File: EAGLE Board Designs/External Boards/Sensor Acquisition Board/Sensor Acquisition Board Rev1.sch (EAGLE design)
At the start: 15 parts, among them U1 ATMEGA328P-AU, X1 CONNECTOR-4NANO-FIT_RIGHT_ANG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

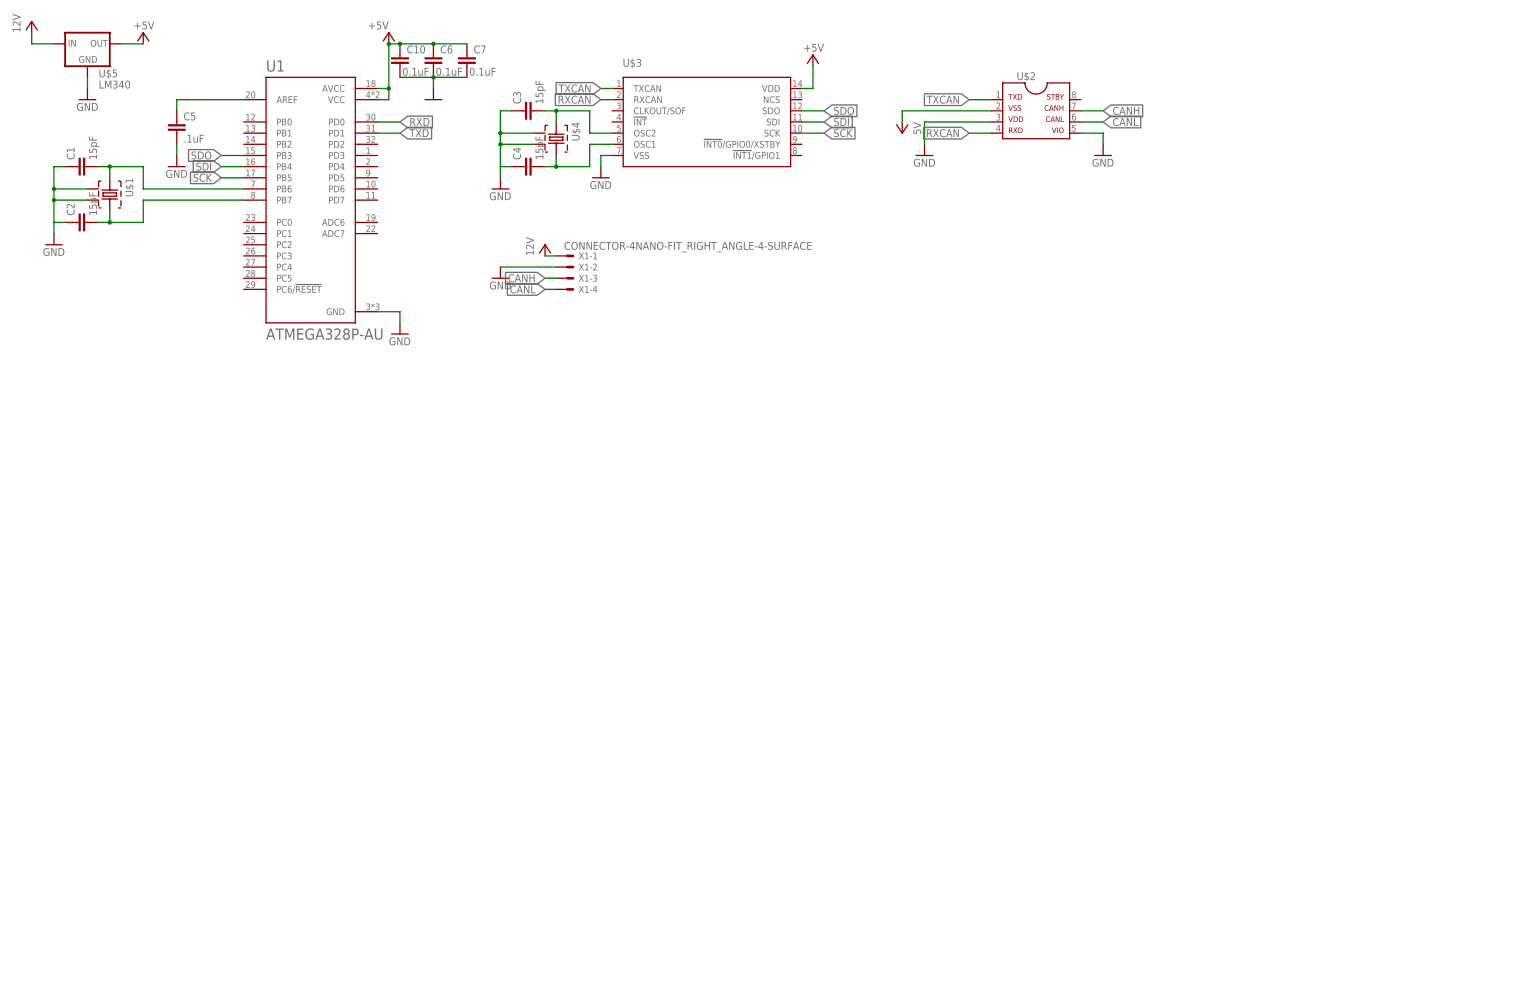
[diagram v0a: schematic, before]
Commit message: Fnished schematic (completed the signal processing portion) and made board
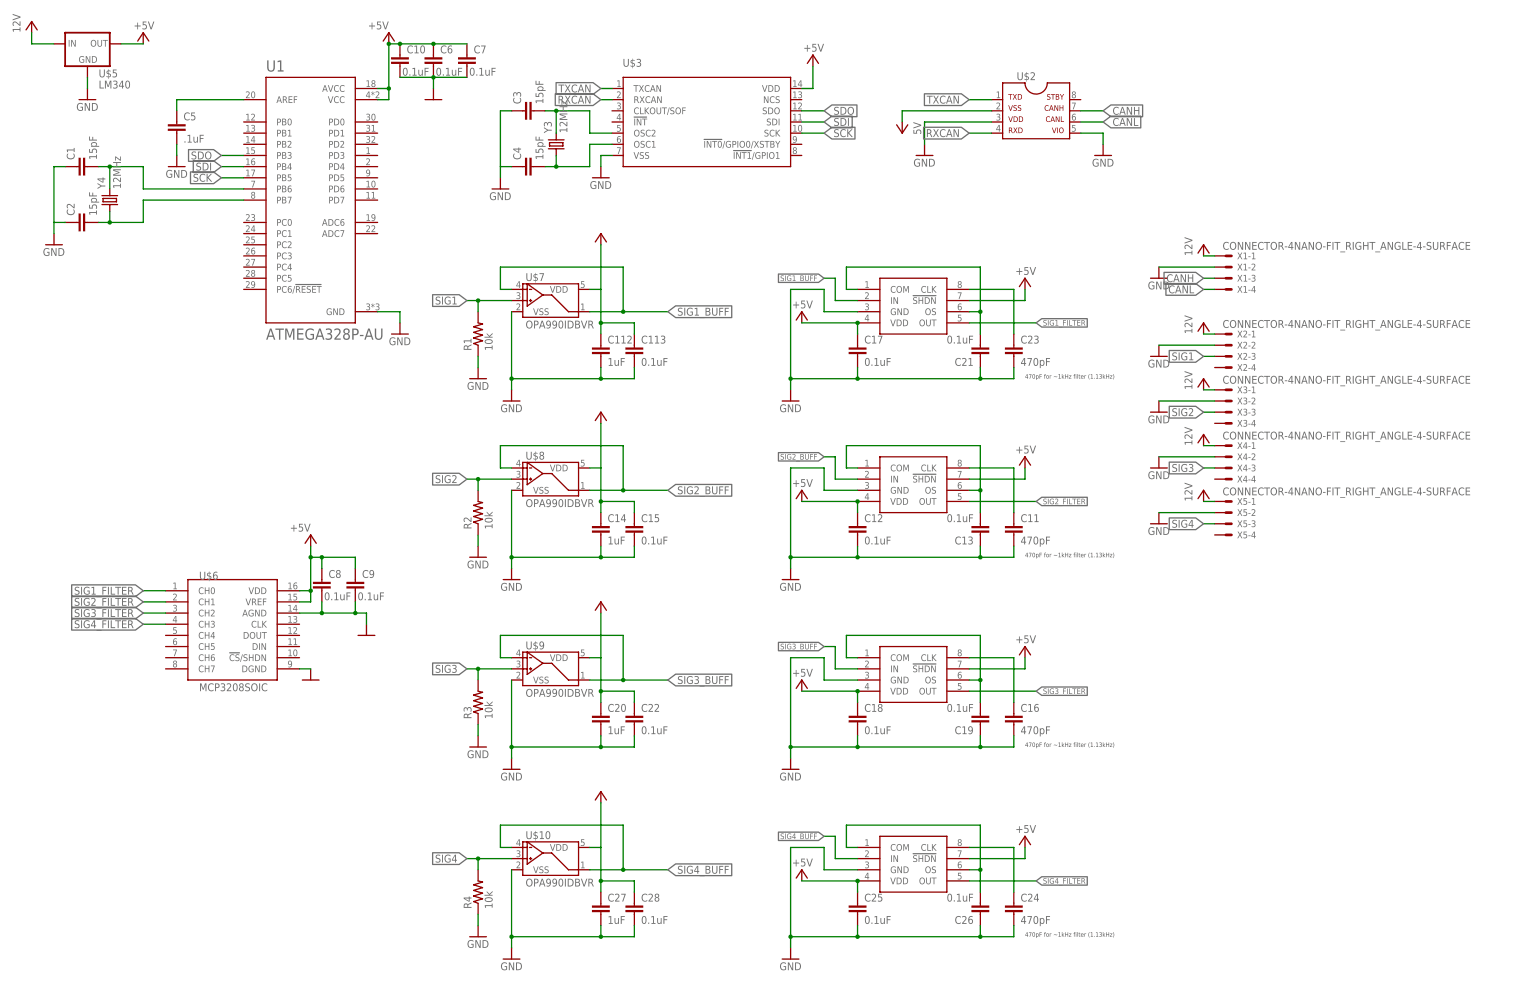
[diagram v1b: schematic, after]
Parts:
- removed U$1, U$4: (no value), HyTechDevices:ABM3B
- added C11, C16, C23, C24: 470pF, HyTechDevices:CAP0603-CAP
- added C112, C14, C20, C27: 1uF, HyTechDevices:CAP0603-CAP
- added C113, C12, C13, C15, C17, C18, C19, C21, C22, C25, C26, C28, C8, C9: 0.1uF, HyTechDevices:CAP0603-CAP
- added R1, R2, R3, R4: 10k, HyTechDevices:RESISTOR1206
- added U$10, U$7, U$8, U$9: OPA990IDBVR, HyTechDevices:OPA990IDBVR
- added U$6: MCP3208SOIC, HyTechDevices:MCP3208SOIC
- added U2, U24, U3, U4: MAX7480, HyTechDevices:MAX7480
- added X2, X3, X4, X5: CONNECTOR-4NANO-FIT_RIGHT_ANGLE-4-SURFACE, HyTechDevices:CONNECTOR-4NANO-FIT_RIGHT_ANGLE-4-SURFACE
- added Y3, Y4: 12MHz, HyTechDevices:CRYSTALCRYSTAL-SMD-5X3-12MHZ
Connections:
- removed net RXD: U1.PD0
- removed net TXD: U1.PD1
- new net N$10: C19.2, U3.COM, U3.OS
- new net N$11: C24.1, U4.CLK
- new net N$12: C26.2, U4.COM, U4.OS
- new net N$136: C23.1, U24.CLK
- new net N$142: C21.2, U24.COM, U24.OS
- new net N$6: C11.1, U2.CLK
- new net N$7: C13.2, U2.COM, U2.OS
- new net N$9: C16.1, U3.CLK
- new net SIG1: R1.2, U$7.VIN+, X2-3.S
- new net SIG1_BUFF: U$7.VIN-, U$7.VOUT, U24.IN
- new net SIG1_FILTER: U$6.CH0, U24.OUT
- new net SIG2: R2.2, U$8.VIN+, X3-3.S
- new net SIG2_BUFF: U$8.VIN-, U$8.VOUT, U2.IN
- new net SIG2_FILTER: U$6.CH1, U2.OUT
- new net SIG3: R3.2, U$9.VIN+, X4-3.S
- new net SIG3_BUFF: U$9.VIN-, U$9.VOUT, U3.IN
- new net SIG3_FILTER: U$6.CH2, U3.OUT
- new net SIG4: R4.2, U$10.VIN+, X5-3.S
- new net SIG4_BUFF: U$10.VIN-, U$10.VOUT, U4.IN
- new net SIG4_FILTER: U$6.CH3, U4.OUT
- net +5V: now also C112.1, C113.1, C12.1, C14.1, C15.1, C17.1, C18.1, C20.1, C22.1, C25.1, C27.1, C28.1, C8.1, C9.1, U$10.VDD, U$6.VDD, U$6.VREF, U$7.VDD, U$8.VDD, U$9.VDD, U2.!SHDN, U2.VDD, U24.!SHDN, U24.VDD, U3.!SHDN, U3.VDD, U4.!SHDN, U4.VDD
- net GND: now also C11.2, C112.2, C113.2, C12.2, C13.1, C14.2, C15.2, C16.2, C17.2, C18.2, C19.1, C20.2, C21.1, C22.2, C23.2, C24.2, C25.2, C26.1, C27.2, C28.2, C8.2, C9.2, R1.1, R2.1, R3.1, R4.1, U$10.VSS, U$6.AGND, U$6.DGND, U$7.VSS, U$8.VSS, U$9.VSS, U2.GND, U24.GND, U3.GND, U4.GND, X2-2.S, X3-2.S, X4-2.S, X5-2.S
- net N$1: no longer U$1.2, U$1.4, U$4.2, U$4.4
- net N$2: now also Y4.2; no longer U$1.1
- net N$3: now also Y4.1; no longer U$1.3
- net N$4: now also Y3.2; no longer U$4.1
- net N$5: now also Y3.1; no longer U$4.3
- net VCC: now also X2-1.S, X3-1.S, X4-1.S, X5-1.S
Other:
- note added: "470pF for ~1kHz filter (1.13kHz)"
- moved on the sheet: X1-1, X1-2, X1-3, X1-4

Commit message: Added controls and connectors
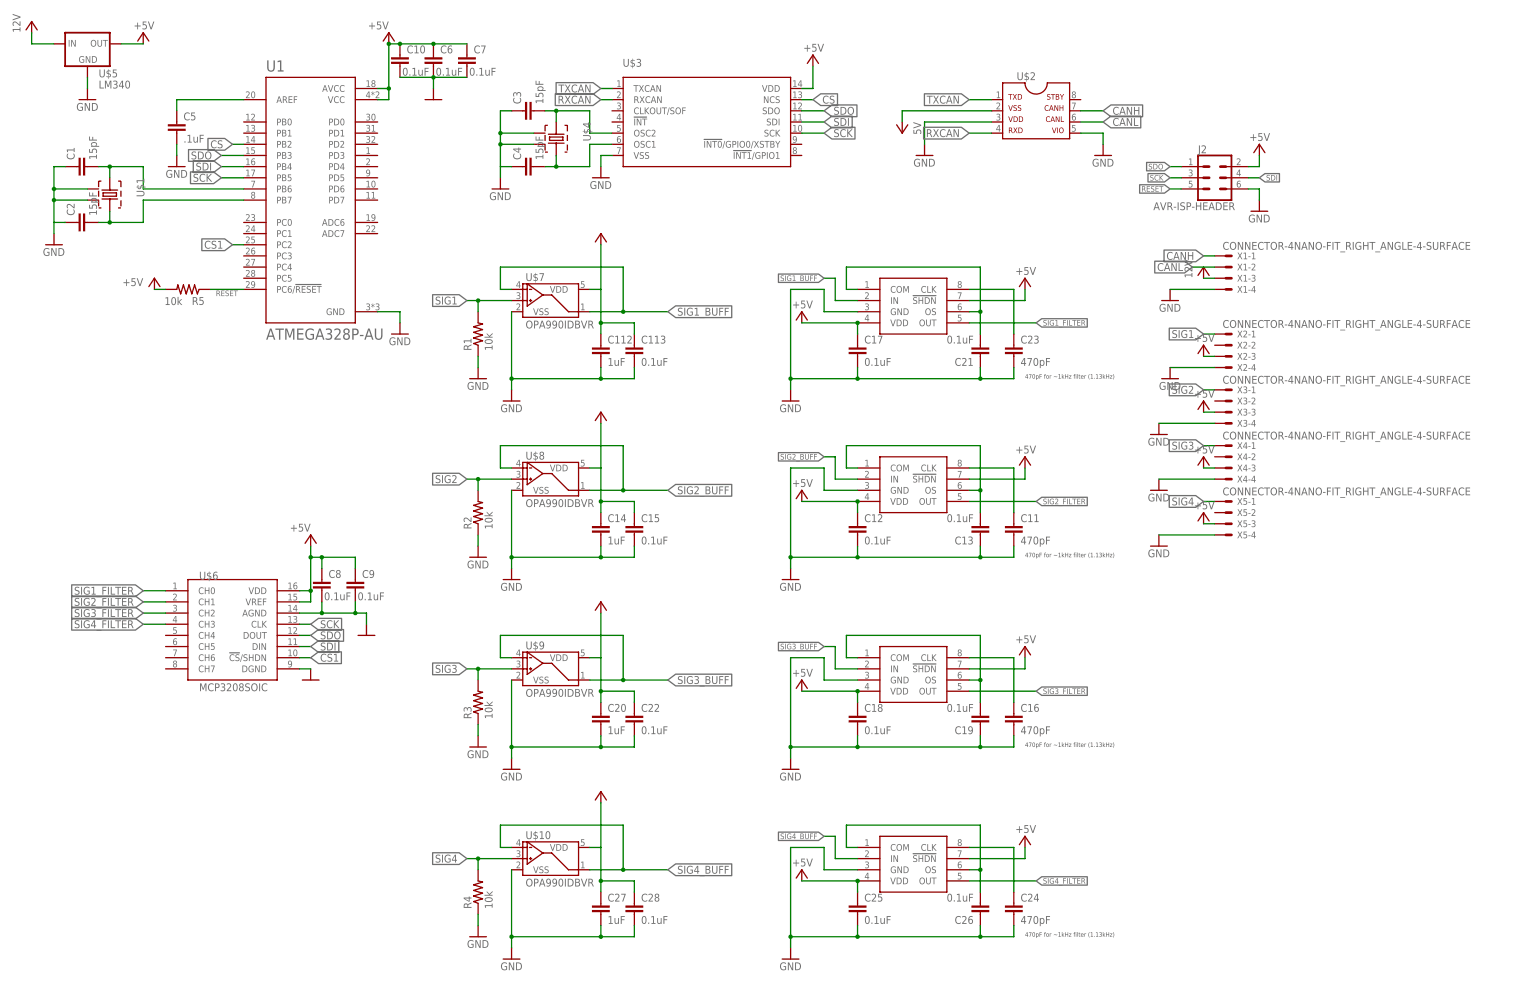
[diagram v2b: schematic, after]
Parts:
- removed Y3, Y4: 12MHz, HyTechDevices:CRYSTALCRYSTAL-SMD-5X3-12MHZ
- added J2: AVR-ISP-HEADER, HyTechDevices:AVR-ISP-HEADER
- added R5: 10k, HyTechDevices:RESISTOR0603
- added U$1, U$4: (no value), HyTechDevices:ABM3B
- C1, C2, C3, C4: device HyTechDevices:CAP1210 -> HyTechDevices:CAP0603-CAP
- R1, R2, R3, R4: device HyTechDevices:RESISTOR1206 -> HyTechDevices:RESISTOR0603
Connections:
- removed net N$1: C1.1, C2.1, C3.1, C4.1
- new net CS: U$3.NCS, U1.PB2
- new net CS1: U$6.!CS!/SHDN, U1.PC2
- new net RESET: J2.5, R5.1, U1.PC6/!RESET
- net +5V: now also J2.2, R5.2, X2-3.S, X3-3.S, X4-3.S, X5-3.S
- net CANH: now also X1-1.S; no longer X1-3.S
- net CANL: now also X1-2.S; no longer X1-4.S
- net GND: now also C1.1, C2.1, C3.1, C4.1, J2.6, U$1.GND, U$1.GND2, U$4.GND, U$4.GND2, X1-4.S, X2-4.S, X3-4.S, X4-4.S, X5-4.S; no longer X1-2.S, X2-2.S, X3-2.S, X4-2.S, X5-2.S
- net N$2: now also U$1.1; no longer Y4.2
- net N$3: now also U$1.3; no longer Y4.1
- net N$4: now also U$4.1; no longer Y3.2
- net N$5: now also U$4.3; no longer Y3.1
- net SCK: now also J2.3, U$6.CLK
- net SDI: now also J2.4, U$6.DIN
- net SDO: now also J2.1, U$6.DOUT
- net SIG1: now also X2-1.S; no longer X2-3.S
- net SIG2: now also X3-1.S; no longer X3-3.S
- net SIG3: now also X4-1.S; no longer X4-3.S
- net SIG4: now also X5-1.S; no longer X5-3.S
- net VCC: now also X1-3.S; no longer X1-1.S, X2-1.S, X3-1.S, X4-1.S, X5-1.S

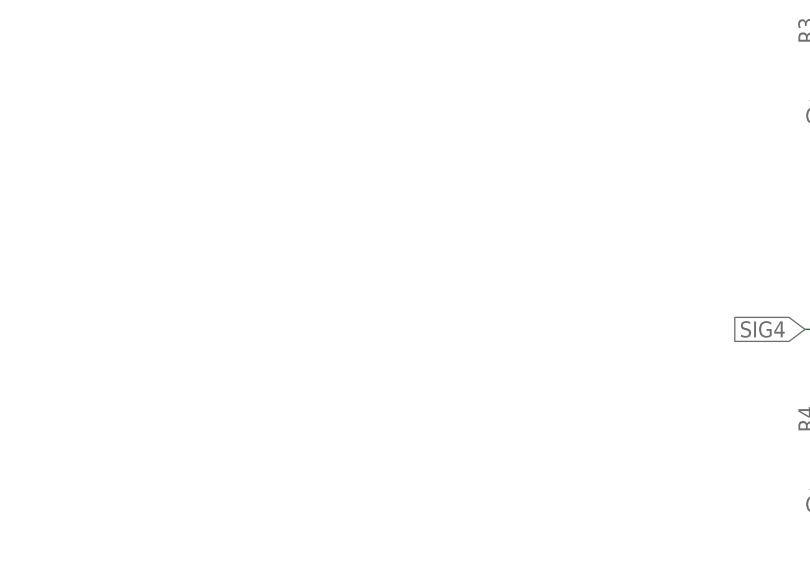
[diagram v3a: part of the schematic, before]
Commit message: Made PCB one sided
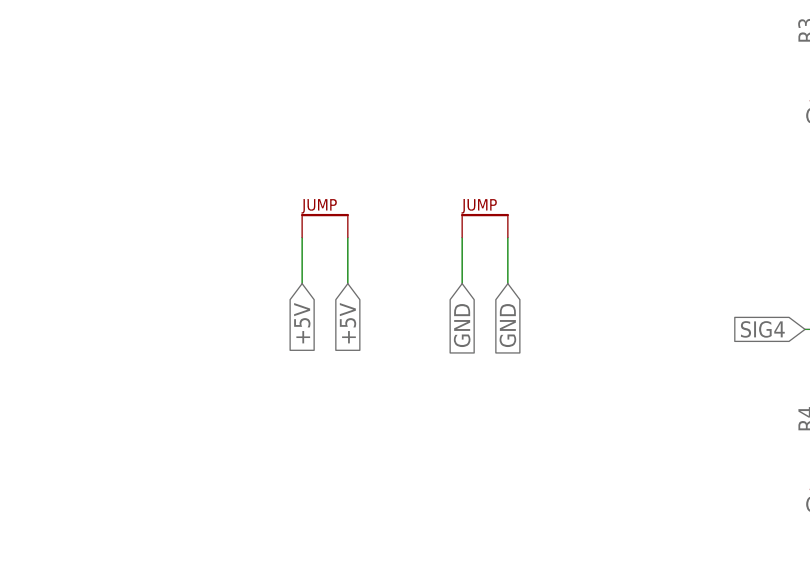
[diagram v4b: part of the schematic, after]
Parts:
- added J1, J3: JUMPER.1, HyTechDevices:JUMPER.1
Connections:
- net +5V: now also J1.P$1, J1.P$2
- net GND: now also J3.P$1, J3.P$2
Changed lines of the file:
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@@
 <part name="P+23" library="HyTechSupplies" deviceset="+5V" device=""/>
 <part name="GND15" library="HyTechSupplies" deviceset="GND" device=""/>
+<part name="J1" library="HyTechDevices" deviceset="JUMPER" device=".1"/>
+<part name="J3" library="HyTechDevices" deviceset="JUMPER" device=".1"/>
 </parts>
 <sheets>
@@
 <attribute name="VALUE" x="248.92" y="-7.62" size="1.778" layer="96"/>
 </instance>
+<instance part="J1" gate="G$1" x="38.1" y="-76.2" smashed="yes"/>
+<instance part="J3" gate="G$1" x="55.88" y="-76.2" smashed="yes"/>
 </instances>
 <busses>
@@
 <pinref part="GND4" gate="1" pin="GND"/>
 </segment>
+<segment>
+<pinref part="J3" gate="G$1" pin="P$1"/>
+<wire x1="55.88" y1="-78.74" x2="55.88" y2="-83.82" width="0.1524" layer="91"/>
+<label x="55.88" y="-83.82" size="1.778" layer="95" rot="R270" xref="yes"/>
+</segment>
+<segment>
+<pinref part="J3" gate="G$1" pin="P$2"/>
+<wire x1="60.96" y1="-78.74" x2="60.96" y2="-83.82" width="0.1524" layer="91"/>
+<label x="60.96" y="-83.82" size="1.778" layer="95" rot="R270" xref="yes"/>
+</segment>
 </net>
 <net name="VCC" class="0">
@@
 <pinref part="P+23" gate="1" pin="+5V"/>
 </segment>
-</net>
+<segment>
+<pinref part="J1" gate="G$1" pin="P$1"/>
+<wire x1="38.1" y1="-78.74" x2="38.1" y2="-83.82" width="0.1524" layer="91"/>
+<label x="38.1" y="-83.82" size="1.778" layer="95" rot="R270" xref="yes"/>
+</segment>
+<segment>
+<pinref part="J1" gate="G$1" pin="P$2"/>
+<wire x1="43.18" y1="-78.74" x2="43.18" y2="-83.82" width="0.1524" layer="91"/>
+<label x="43.18" y="-83.82" size="1.778" layer="95" rot="R270" xref="yes"/>
+</segment>
+</net>
